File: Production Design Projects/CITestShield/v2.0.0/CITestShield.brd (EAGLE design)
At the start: 53.3 x 54.6 mm, 36 parts, among them CON1 MICRO-SD, IC4 LM75BD, SW1 SPST-4_TP1154_J

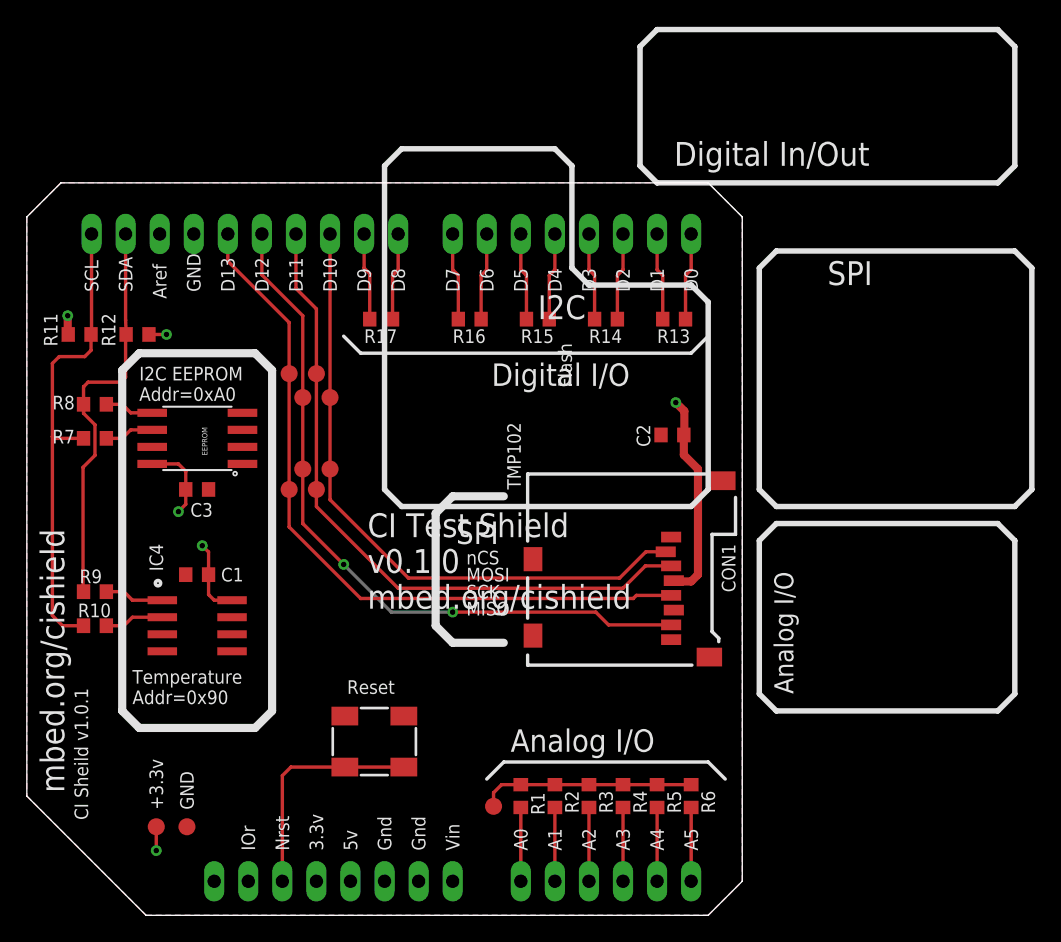
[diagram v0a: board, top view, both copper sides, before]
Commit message: Release of v2.0.0 CI test shield, removal of R13(UART Tests Removed)
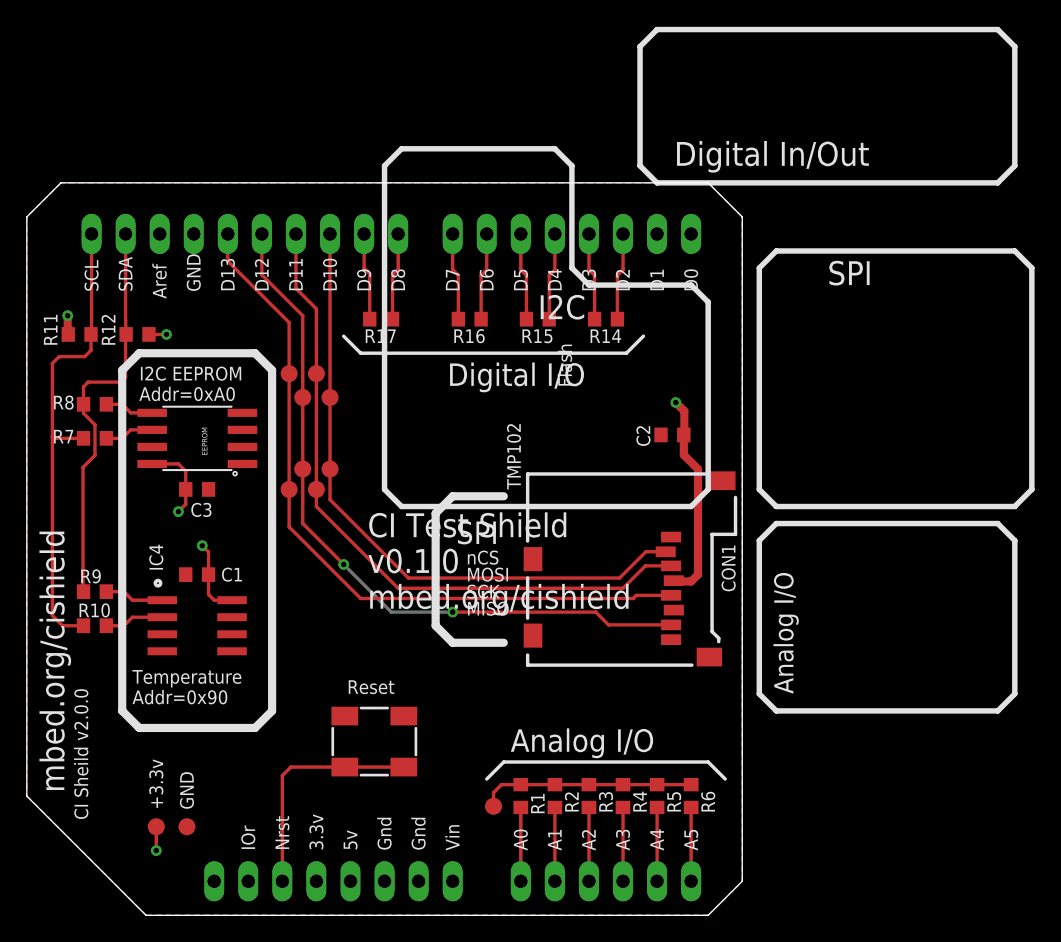
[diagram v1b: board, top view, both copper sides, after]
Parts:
- removed R13: 0R, mbed-HDK:0603
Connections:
- removed net N$12: BRD1.16, R13.2
- removed net N$13: BRD1.15, R13.1
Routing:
- net N$13: track 6.52 -> 0.00 mm
- net N$12: track 6.52 -> 0.00 mm
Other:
- board text added: "CI Sheild v2.0.0"
- board text removed: "CI Sheild v1.0.1"
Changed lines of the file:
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@@
 <?xml version="1.0" encoding="utf-8"?>
 <!DOCTYPE eagle SYSTEM "eagle.dtd">
-<eagle version="7.3.0">
+<eagle version="7.6.0">
 <drawing>
 <settings>
@@
 <text x="30.988" y="4.826" size="1.016" layer="21" font="vector" ratio="12" rot="R90">IOr</text>
 <wire x1="37.592" y1="43.18" x2="38.862" y2="41.91" width="0.254" layer="21"/>
-<wire x1="38.862" y1="41.91" x2="63.5" y2="41.91" width="0.254" layer="21"/>
-<wire x1="63.5" y1="41.91" x2="64.77" y2="43.18" width="0.254" layer="21"/>
+<wire x1="38.862" y1="41.91" x2="58.674" y2="41.91" width="0.254" layer="21"/>
+<wire x1="58.674" y1="41.91" x2="59.944" y2="43.18" width="0.254" layer="21"/>
 <wire x1="48.26" y1="10.16" x2="49.53" y2="11.43" width="0.254" layer="21"/>
 <wire x1="49.53" y1="11.43" x2="64.77" y2="11.43" width="0.254" layer="21"/>
 <wire x1="64.77" y1="11.43" x2="66.04" y2="10.16" width="0.254" layer="21"/>
 <text x="50.038" y="12.192" size="1.6764" layer="21" font="vector" ratio="12">Analog I/O</text>
-<text x="58.928" y="41.148" size="1.6764" layer="21" font="vector" ratio="12" rot="R180">Digital I/O</text>
+<text x="55.626" y="41.148" size="1.6764" layer="21" font="vector" ratio="12" rot="R180">Digital I/O</text>
 <text x="45.974" y="27.686" size="1.6764" layer="21" font="vector" ratio="12">SPI</text>
 <text x="46.736" y="26.162" size="1.016" layer="21" font="vector" ratio="12">nCS</text>
@@
 <text x="22.352" y="38.354" size="1.016" layer="21" font="vector" ratio="12">Addr=0xA0</text>
 <text x="21.844" y="15.748" size="1.016" layer="21" font="vector" ratio="12">Addr=0x90</text>
-<text x="18.542" y="7.112" size="1.016" layer="21" ratio="12" rot="R90">CI Sheild v1.0.1</text>
+<text x="18.542" y="7.112" size="1.016" layer="21" ratio="12" rot="R90">CI Sheild v2.0.0</text>
 <text x="60.96" y="43.18" size="1.6764" layer="22" ratio="12" rot="MR0">Tests :</text>
 <text x="58.42" y="40.64" size="1.016" layer="22" ratio="12" rot="MR0">Analog I/O - A0-5 mesh</text>
@@
 <attribute name="VALUE" x="33.782" y="18.542" size="1.016" layer="27" font="vector" ratio="12" rot="R90"/>
 </element>
-<element name="R13" library="mbed-HDK" package="0603" value="0R" x="62.23" y="44.45" locked="yes" smashed="yes" rot="R180">
-<attribute name="NAME" x="60.96" y="42.672" size="1.016" layer="25" font="vector" ratio="12"/>
-<attribute name="VALUE" x="63.246" y="40.386" size="1.016" layer="27" font="vector" ratio="12" rot="R90"/>
-</element>
 <element name="R14" library="mbed-HDK" package="0603" value="0R" x="57.15" y="44.45" locked="yes" smashed="yes" rot="R180">
 <attribute name="NAME" x="55.88" y="42.672" size="1.016" layer="25" font="vector" ratio="12"/>
@@
 <wire x1="41.656" y1="48.133" x2="41.656" y2="50.8" width="0.254" layer="1"/>
 </signal>
-<signal name="N$12">
-<contactref element="BRD1" pad="16"/>
-<contactref element="R13" pad="2"/>
-<wire x1="61.38" y1="44.45" x2="61.38" y2="47.713" width="0.254" layer="1"/>
-<wire x1="61.38" y1="47.713" x2="60.96" y2="48.133" width="0.254" layer="1"/>
-<wire x1="60.96" y1="48.133" x2="60.96" y2="50.8" width="0.254" layer="1"/>
-</signal>
-<signal name="N$13">
-<contactref element="BRD1" pad="15"/>
-<contactref element="R13" pad="1"/>
-<wire x1="63.08" y1="44.45" x2="63.08" y2="47.713" width="0.254" layer="1"/>
-<wire x1="63.08" y1="47.713" x2="63.5" y2="48.133" width="0.254" layer="1"/>
-<wire x1="63.5" y1="48.133" x2="63.5" y2="50.8" width="0.254" layer="1"/>
-</signal>
 <signal name="N$14">
